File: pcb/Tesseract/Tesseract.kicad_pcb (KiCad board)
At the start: 2 copper layers, 67 x 55 mm, 31 parts, among them IC1 MAX98357AETE+T, J1 NHD-1.91-176176UBC3 Conn-1, J2 USB C Power Connector, J3 Speaker Connector, J4 RPI Power Connector, J5 LED Strip Connector, J6 RPI Signal Connector 1, J7 RPI Signal Connector 2, J8 NHD-1.91-176176UBC3 Conn-2, SW1 SW_Push, SW2 SW_Push, SW3 SW_Push, SW4 SW_Push

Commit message: Add yesterday's work to journal
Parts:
- moved J4 56.6 mm to (54.0, 63.8)
- moved C9 37.7 mm to (85.2, 99.5), turned to -90 degrees
- moved C10 35.1 mm to (83.2, 99.5), turned to -90 degrees
- moved REF** 24.1 mm to (114.0, 114.0)
- moved REF** 24.0 mm to (54.8, 114.0)
- moved SW4 19.8 mm to (111.9, 98.4), turned to 90 degrees
- moved J8 19.8 mm to (62.5, 113.3)
- moved C5 18.0 mm to (83.0, 70.5)
- moved C8 18.0 mm to (87.5, 70.5)
- moved C6 17.1 mm to (83.0, 68.5)
- moved C7 17.1 mm to (87.5, 68.5)
- moved R1 15.7 mm to (116.2, 107.2), turned to -90 degrees
- moved C4 13.7 mm to (65.8, 100.0), turned to -90 degrees
- moved J2 13.5 mm to (112.0, 63.8)
- moved R2 13.3 mm to (116.2, 103.5), turned to -90 degrees
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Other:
- board size 67 x 55 mm -> 68.8 x 68.8 mm
- board text added: "+5V"
- board text added: "BCLK"
- board text added: "CS#"
- board text added: "D/C#"
- board text added: "DIN"
- board text added: "GND"
- board text added: "IC1"
- board text added: "LED_DIN"
- board text added: "LRCLK"
- board text added: "NC"
- board text added: "RES#"
- board text added: "SCK"
- board text added: "SCLK"
- board text added: "SD"
- board text added: "SDIN"
- board text added: "SW1"
- board text added: "SW2"
- board text added: "SW3"
- board text added: "SW4"
- board text added: "WS"

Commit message: Log work from a couple of days ago in journal
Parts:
- added REF**: MountingHole_3.2mm_M3_Pad_TopBottom, MountingHole:MountingHole_3.2mm_M3_Pad_TopBottom, F.Cu at (67.5, 84.2)
- added REF**: MountingHole_3.2mm_M3_Pad_TopBottom, MountingHole:MountingHole_3.2mm_M3_Pad_TopBottom, F.Cu at (98.5, 84.2)
- C4: value 0.1u -> 10u
- J4: footprint Connector_JST:JST_XH_B2B-XH-A_1x02_P2.50mm_Vertical -> Connector_JST:JST_XH_B3B-XH-A_1x03_P2.50mm_Vertical
- moved C3 2.50 mm to (63.5, 102.5)
- moved C4 2.50 mm to (65.8, 102.5), turned to 90 degrees
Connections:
- C4 pad 1: GND -> +5V
- C4 pad 2: +5V -> GND
- J4 pad 2: GND -> +3V3
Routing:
- net +3V3: track 0.00 -> 132.4 mm, vias 0 -> 2
- net SW4: track 0.00 -> 85.6 mm
- net D/C#: track 0.00 -> 73.2 mm
- net LED_DIN: track 0.00 -> 72.4 mm, vias 0 -> 1
- net RES#: track 0.00 -> 71.5 mm
- net WS: track 0.00 -> 71.4 mm
- net SW3: track 0.00 -> 69.3 mm
- net CS#: track 0.00 -> 65.6 mm
- net BCLK: track 0.00 -> 63.6 mm, vias 0 -> 2
- net LRCLK: track 0.00 -> 61.3 mm, vias 0 -> 1
- net SCLK: track 0.00 -> 60.2 mm
- net DIN: track 0.00 -> 57.9 mm, vias 0 -> 1
- net SDIN: track 0.00 -> 57.4 mm
- net SCK: track 0.00 -> 54.7 mm, vias 0 -> 2
- net GND: track 0.00 -> 50.8 mm, vias 0 -> 13
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- added copper zone on F.Cu, net +5V
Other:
- outline, holes or cut-outs redrawn
- board text added: "+3V3"
- board text added: "OUTN"
- board text added: "OUTP"

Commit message: Add yesterday's work and journal entry
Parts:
- J5: moved to F.Cu
- moved REF** 10.6 mm to (102.4, 94.1)
- moved REF** 9.69 mm to (66.4, 74.6)
- moved REF** 0.50 mm to (54.8, 55.2)
- moved REF** 0.50 mm to (114.0, 55.2)
- moved SW1 0.45 mm to (56.9, 70.8)
- moved SW2 0.45 mm to (56.9, 92.3)
- moved SW3 0.25 mm to (111.9, 77.1)
- moved SW4 0.25 mm to (111.9, 98.6)
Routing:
- net GND: track 50.8 -> 52.3 mm
- net LRCLK: track 61.3 -> 60.0 mm
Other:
- board size 68.8 x 68.8 mm -> 68.8 x 68.2 mm
- board text added: "Tesseract"
- board text added: "by @crkalapat"
- board text added: "v1.0"

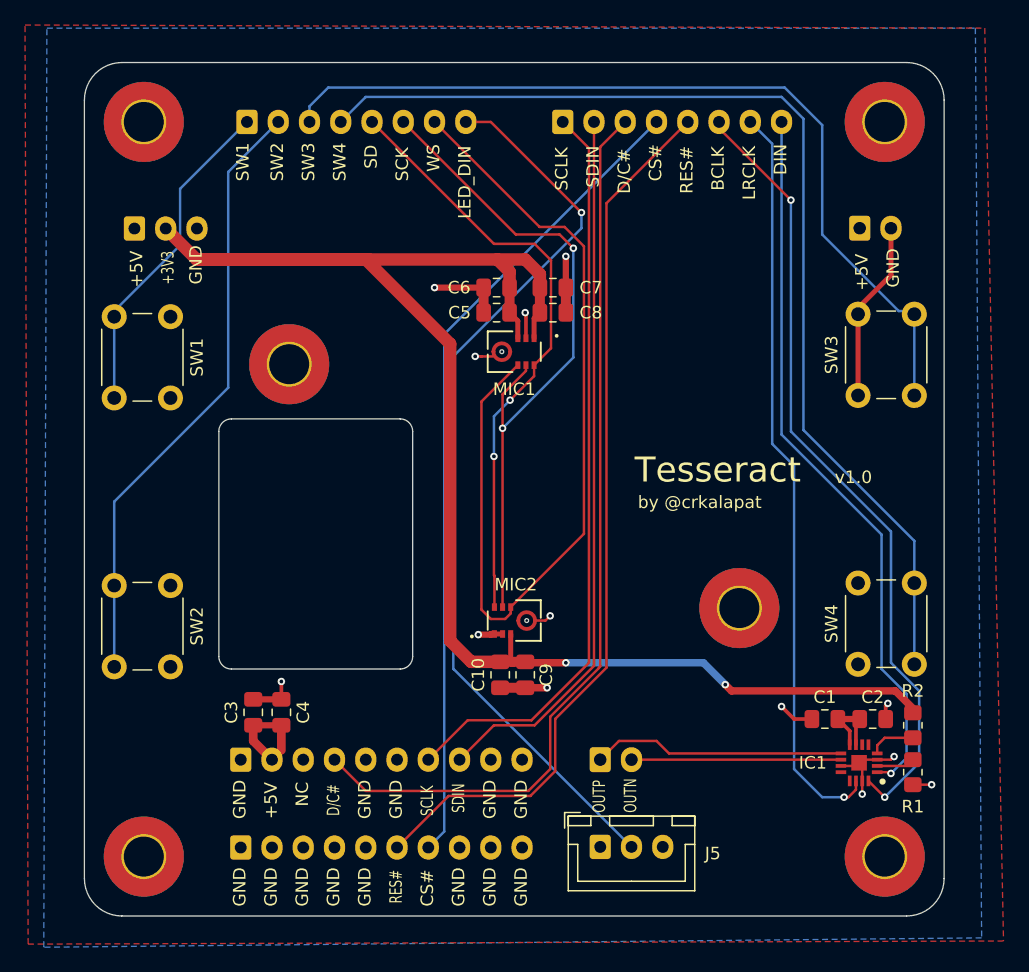
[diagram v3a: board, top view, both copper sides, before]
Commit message: Remove top mic from PCB and schematic
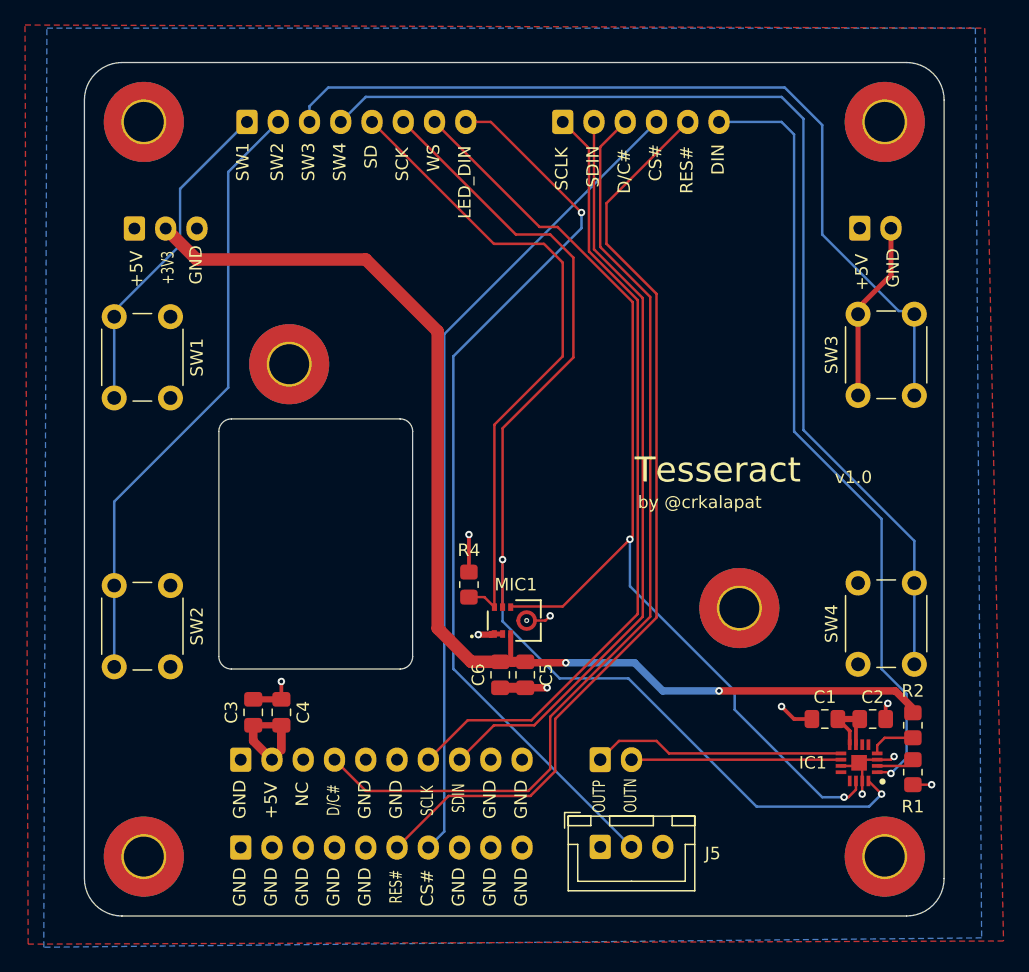
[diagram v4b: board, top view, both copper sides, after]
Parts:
- removed the C5 at (83.0, 70.5)
- removed the C6 at (83.0, 68.5)
- removed C7: 0.1u, Capacitor_SMD:C_0805_2012Metric_Pad1.18x1.45mm_HandSolder
- removed C8: 10u, Capacitor_SMD:C_0805_2012Metric_Pad1.18x1.45mm_HandSolder
- removed the MIC1 at (84.4, 73.6)
- added R4: 100k, Resistor_SMD:R_0805_2012Metric_Pad1.20x1.40mm_HandSolder, F.Cu at (80.8, 92.2)
- J6: footprint Connector_JST:JST_XH_B8B-XH-A_1x08_P2.50mm_Vertical -> Connector_JST:JST_XH_B6B-XH-A_1x06_P2.50mm_Vertical
- renumbered C9 to C5, C10 to C6, MIC2 to MIC1
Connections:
- IC1 pad 14: LRCLK -> WS
- IC1 pad 16: BCLK -> SCK
- J6 pad 6: BCLK -> DIN
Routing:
- net BCLK: track 63.6 -> 0.00 mm, vias 2 -> 0
- net LRCLK: track 60.0 -> 0.00 mm, vias 1 -> 0
- net +3V3: track 132.4 -> 92.2 mm
- net SCK: track 54.7 -> 91.7 mm
- net WS: track 71.4 -> 83.3 mm, vias 0 -> 2
- net GND: track 52.3 -> 41.4 mm, vias 13 -> 10
- net DIN: track 57.9 -> 63.4 mm
- net SD: track 48.5 -> 52.1 mm, vias 2 -> 0
- net RES#: track 71.5 -> 74.8 mm
- net D/C#: track 73.2 -> 76.6 mm
- net SCLK: track 60.2 -> 63.4 mm
- net SDIN: track 57.4 -> 60.6 mm
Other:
- board text removed: "BCLK"
- board text removed: "LRCLK"

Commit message: Change PCB and schematic connectors for easier wiring
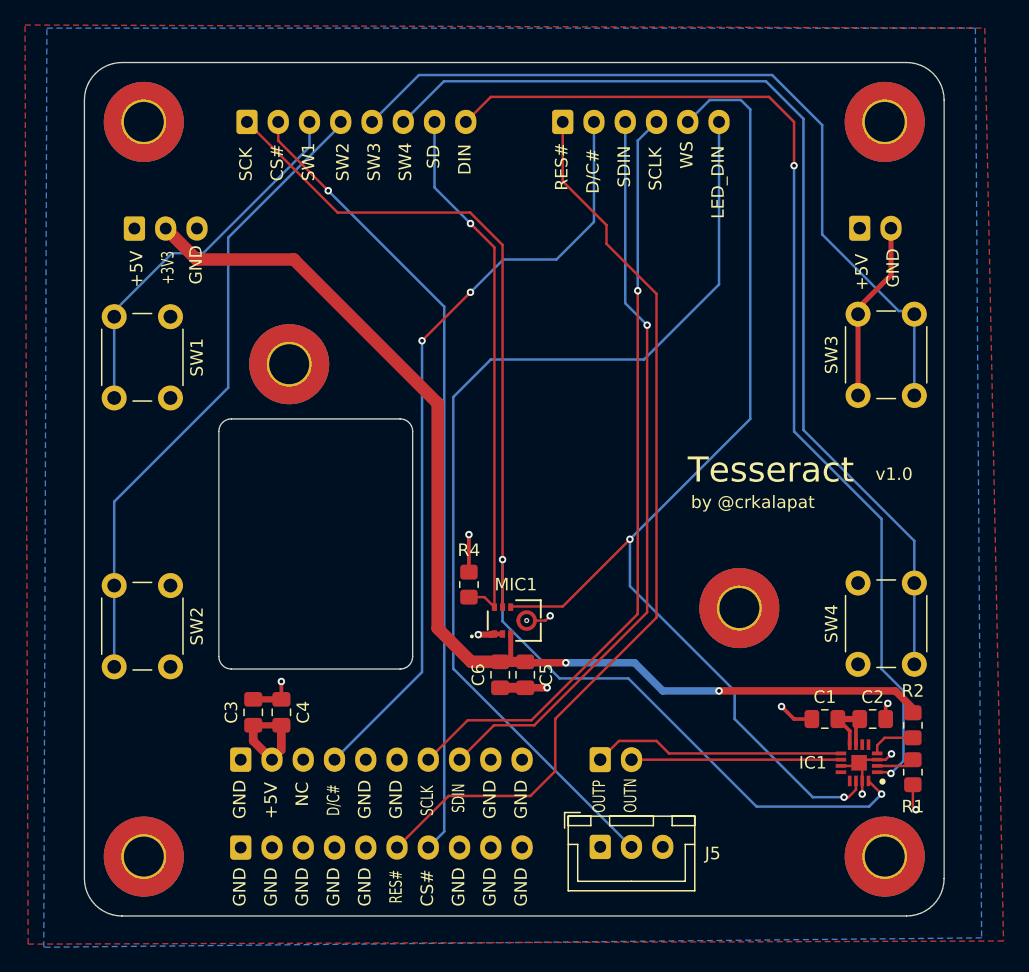
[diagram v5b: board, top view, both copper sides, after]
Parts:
- R2: value 634k -> 210k
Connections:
- J6 pad 1: SCLK -> RES#
- J6 pad 2: SDIN -> D/C#
- J6 pad 3: D/C# -> SDIN
- J6 pad 4: CS# -> SCLK
- J6 pad 5: RES# -> WS
- J6 pad 6: DIN -> LED_DIN
- J7 pad 1: SW1 -> SCK
- J7 pad 2: SW2 -> CS#
- J7 pad 3: SW3 -> SW1
- J7 pad 4: SW4 -> SW2
- J7 pad 5: SD -> SW3
- J7 pad 6: SCK -> SW4
- J7 pad 7: WS -> SD
- J7 pad 8: LED_DIN -> DIN
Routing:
- net DIN: track 63.4 -> 85.2 mm, vias 1 -> 2
- net D/C#: track 76.6 -> 62.1 mm, vias 0 -> 2
- net SD: track 52.1 -> 43.2 mm, vias 0 -> 1
- net LED_DIN: track 72.4 -> 80.4 mm, vias 1 -> 0
- net SCK: track 91.7 -> 96.8 mm
- net SW3: track 69.3 -> 64.4 mm
- net WS: track 83.3 -> 87.3 mm
- net SW4: track 85.6 -> 81.6 mm
- net SW1: track 26.0 -> 29.6 mm
- net +3V3: track 92.2 -> 88.8 mm
- net SW2: track 48.6 -> 50.6 mm
- net SCLK: track 63.4 -> 61.5 mm, vias 0 -> 1
- net CS#: track 65.6 -> 64.1 mm, vias 0 -> 1
- net RES#: track 74.8 -> 73.6 mm
- net SDIN: track 60.6 -> 59.8 mm, vias 0 -> 1

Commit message: Update PCB and schematic connections and wiring
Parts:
- J1, J8: footprint Connector_JST:JST_XH_B10B-XH-A_1x10_P2.50mm_Vertical -> Connector_JST:JST_XH_B10B-XH-AM_1x10_P2.50mm_Vertical
- J7: footprint Connector_JST:JST_XH_B8B-XH-A_1x08_P2.50mm_Vertical -> Connector_JST:JST_XH_B8B-XH-AM_1x08_P2.50mm_Vertical
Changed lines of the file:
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@@
 			(outputformat 1)
 			(mirror no)
-			(drillshape 1)
+			(drillshape 0)
 			(scaleselection 1)
-			(outputdirectory "")
+			(outputdirectory "../production/")
 		)
 	)
@@
 		)
 	)
-	(footprint "Connector_JST:JST_XH_B10B-XH-A_1x10_P2.50mm_Vertical"
+	(footprint "Connector_JST:JST_XH_B10B-XH-AM_1x10_P2.50mm_Vertical"
 		(layer "B.Cu")
 		(at 62.5 106.25)
-		(descr "JST XH series connector, B10B-XH-A (http://www.jst-mfg.com/product/pdf/eng/eXH.pdf), generated with kicad-footprint-generator")
-		(tags "connector JST XH vertical")
+		(descr "JST XH series connector, B10B-XH-AM, with boss (http://www.jst-mfg.com/product/pdf/eng/eXH.pdf), generated with kicad-footprint-generator")
+		(tags "connector JST XH vertical boss")
 		(property "Reference" "J1"
-			(at 11.25 -4.75 180)
+			(at 11.25 3.55 180)
 			(layer "B.SilkS")
 			(effects
@@
 			)
 		)
-		(property "Description" "Generic connector, single row, 01x10, script generated"
+		(property "Description" ""
 			(at 0 0 180)
 			(layer "B.Fab")
@@
 		)
 		(fp_line
-			(start -1.8 -2.75)
-			(end 11.25 -2.75)
-			(stroke
-				(width 0.12)
-				(type solid)
-			)
-			(layer "B.SilkS")
-		)
-		(fp_line
 			(start -1.8 0.2)
-			(end -1.8 -2.75)
+			(end -1.8 -1.14)
 			(stroke
 				(width 0.12)
@@
 		)
 		(fp_line
+			(start 11.25 -2.75)
+			(end -0.74 -2.75)
+			(stroke
+				(width 0.12)
+				(type solid)
+			)
+			(layer "B.SilkS")
+		)
+		(fp_line
 			(start 21.75 1.7)
 			(end 21.75 2.45)
@@
 			)
 		)
+		(pad "" np_thru_hole circle
+			(at -1.6 -2)
+			(size 1.2 1.2)
+			(drill 1.2)
+			(layers "*.Cu" "*.Mask")
+		)
 		(pad "1" thru_hole roundrect
 			(at 0 0)
@@
 		)
 		(embedded_fonts no)
-		(model "${KICAD9_3DMODEL_DIR}/Connector_JST.3dshapes/JST_XH_B10B-XH-A_1x10_P2.50mm_Vertical.step"
+		(model "${KICAD9_3DMODEL_DIR}/Connector_JST.3dshapes/JST_XH_B10B-XH-AM_1x10_P2.50mm_Vertical.step"
 			(offset
 				(xyz 0 0 0)
@@
 		)
 	)
-	(footprint "Connector_JST:JST_XH_B10B-XH-A_1x10_P2.50mm_Vertical"
+	(footprint "Connector_JST:JST_XH_B10B-XH-AM_1x10_P2.50mm_Vertical"
 		(layer "B.Cu")
 		(at 62.5 113.275)
-		(descr "JST XH series connector, B10B-XH-A (http://www.jst-mfg.com/product/pdf/eng/eXH.pdf), generated with kicad-footprint-generator")
-		(tags "connector JST XH vertical")
+		(descr "JST XH series connector, B10B-XH-AM, with boss (http://www.jst-mfg.com/product/pdf/eng/eXH.pdf), generated with kicad-footprint-generator")
+		(tags "connector JST XH vertical boss")
 		(property "Reference" "J8"
-			(at 11.25 3.725 180)
+			(at 11.25 3.55 180)
 			(layer "B.SilkS")
 			(effects
@@
 			)
 		)
-		(property "Description" "Generic connector, single row, 01x10, script generated"
+		(property "Description" ""
 			(at 0 0 180)
 			(layer "B.Fab")
@@
 		)
 		(fp_line
-			(start -1.8 -2.75)
-			(end 11.25 -2.75)
-			(stroke
-				(width 0.12)
-				(type solid)
-			)
-			(layer "B.SilkS")
-		)
-		(fp_line
 			(start -1.8 0.2)
-			(end -1.8 -2.75)
+			(end -1.8 -1.14)
 			(stroke
 				(width 0.12)
@@
 		)
 		(fp_line
+			(start 11.25 -2.75)
+			(end -0.74 -2.75)
+			(stroke
+				(width 0.12)
+				(type solid)
+			)
+			(layer "B.SilkS")
+		)
+		(fp_line
 			(start 21.75 1.7)
 			(end 21.75 2.45)
@@
 			)
 		)
+		(pad "" np_thru_hole circle
+			(at -1.6 -2)
+			(size 1.2 1.2)
+			(drill 1.2)
+			(layers "*.Cu" "*.Mask")
+		)
 		(pad "1" thru_hole roundrect
 			(at 0 0)
@@
 		)
 		(embedded_fonts no)
-		(model "${KICAD9_3DMODEL_DIR}/Connector_JST.3dshapes/JST_XH_B10B-XH-A_1x10_P2.50mm_Vertical.step"
+		(model "${KICAD9_3DMODEL_DIR}/Connector_JST.3dshapes/JST_XH_B10B-XH-AM_1x10_P2.50mm_Vertical.step"
 			(offset
 				(xyz 0 0 0)
@@
 		)
 	)
-	(footprint "Connector_JST:JST_XH_B8B-XH-A_1x08_P2.50mm_Vertical"
+	(footprint "Connector_JST:JST_XH_B8B-XH-AM_1x08_P2.50mm_Vertical"
 		(layer "B.Cu")
 		(at 63 55.25)
-		(descr "JST XH series connector, B8B-XH-A (http://www.jst-mfg.com/product/pdf/eng/eXH.pdf), generated with kicad-footprint-generator")
-		(tags "connector JST XH vertical")
+		(descr "JST XH series connector, B8B-XH-AM, with boss (http://www.jst-mfg.com/product/pdf/eng/eXH.pdf), generated with kicad-footprint-generator")
+		(tags "connector JST XH vertical boss")
 		(property "Reference" "J7"
-			(at 8.75 3.75 180)
+			(at 8.75 3.55 180)
 			(layer "B.SilkS")
 			(effects
@@
 			)
 		)
-		(property "Description" "Generic connector, single row, 01x08, script generated"
+		(property "Description" ""
 			(at 0 0 180)
 			(layer "B.Fab")
@@
 		)
 		(fp_line
-			(start -1.8 -2.75)
-			(end 8.75 -2.75)
-			(stroke
-				(width 0.12)
-				(type solid)
-			)
-			(layer "B.SilkS")
-		)
-		(fp_line
 			(start -1.8 0.2)
-			(end -1.8 -2.75)
+			(end -1.8 -1.14)
 			(stroke
 				(width 0.12)
@@
 		)
 		(fp_line
+			(start 8.75 -2.75)
+			(end -0.74 -2.75)
+			(stroke
+				(width 0.12)
+				(type solid)
+			)
+			(layer "B.SilkS")
+		)
+		(fp_line
 			(start 16.75 1.7)
 			(end 16.75 2.45)
@@
 			)
 		)
+		(pad "" np_thru_hole circle
+			(at -1.6 -2)
+			(size 1.2 1.2)
+			(drill 1.2)
+			(layers "*.Cu" "*.Mask")
+		)
 		(pad "1" thru_hole roundrect
 			(at 0 0)
@@
 		)
 		(embedded_fonts no)
-		(model "${KICAD9_3DMODEL_DIR}/Connector_JST.3dshapes/JST_XH_B8B-XH-A_1x08_P2.50mm_Vertical.step"
+		(model "${KICAD9_3DMODEL_DIR}/Connector_JST.3dshapes/JST_XH_B8B-XH-AM_1x08_P2.50mm_Vertical.step"
 			(offset
 				(xyz 0 0 0)

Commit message: Update PCB and schematic related files
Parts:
- J1, J8: footprint Connector_JST:JST_XH_B10B-XH-AM_1x10_P2.50mm_Vertical -> Connector_JST:JST_XH_B10B-XH-A_1x10_P2.50mm_Vertical
- J6: footprint Connector_JST:JST_XH_B6B-XH-A_1x06_P2.50mm_Vertical -> Connector_JST:JST_XH_B7B-XH-A_1x07_P2.50mm_Vertical
- J7: footprint Connector_JST:JST_XH_B8B-XH-AM_1x08_P2.50mm_Vertical -> Connector_JST:JST_XH_B7B-XH-A_1x07_P2.50mm_Vertical
- moved J6 2.50 mm to (85.8, 55.2)
- moved REF** 1.98 mm to (103.0, 96.0)
- moved REF** 1.67 mm to (66.0, 73.0)
- moved R4 1.50 mm to (80.8, 93.8)
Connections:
- J6 pad 1: RES# -> DIN
- J6 pad 2: D/C# -> RES#
- J6 pad 3: SDIN -> D/C#
- J6 pad 4: SCLK -> SDIN
- J6 pad 5: WS -> SCLK
- J6 pad 6: LED_DIN -> WS
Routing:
- net DIN: track 85.2 -> 80.4 mm
- net GND: track 41.9 -> 40.6 mm
- net SCK: track 96.8 -> 96.3 mm
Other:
- outline, holes or cut-outs redrawn
- board text added: "LED Strip"
